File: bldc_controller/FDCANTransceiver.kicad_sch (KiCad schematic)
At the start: 4 parts, among them U9 TCAN1051HGVDRBRQ1

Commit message: might have fixed net issue, added dxf and svgs
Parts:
- gave numbers to parts that had none: 1
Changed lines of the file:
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@@
-    (stroke (width 0) (type default))
-  )
-  (polyline (pts (xy 99.06 55.88) (xy 99.06 130.81))
     (stroke (width 0) (type default))
   )
@@
     (stroke (width 0) (type default))
   )
-  (polyline (pts (xy 102.87 52.07) (xy 195.58 52.07))
-    (stroke (width 0) (type default))
-  )
-  (polyline (pts (xy 199.39 55.88) (xy 199.39 130.81))
-    (stroke (width 0) (type default))
-  )
   (wire (pts (xy 167.64 71.12) (xy 167.64 67.31))
     (stroke (width 0) (type default))
@@
     (stroke (width 0) (type default))
   )
-  (polyline (pts (xy 195.58 134.62) (xy 102.87 134.62))
-    (stroke (width 0) (type default))
-  )
   (bus (pts (xy 184.15 86.36) (xy 179.07 86.36))
     (stroke (width 0) (type default))
@@
     (stroke (width 0) (type default))
   )
+  (polyline (pts (xy 116.84 101.6) (xy 123.19 109.22))
+    (stroke (width 0) (type dot) (color 255 0 0 1))
+  )
   (wire (pts (xy 132.08 67.31) (xy 147.32 67.31))
     (stroke (width 0) (type default))
   )
-  (arc (start 102.87 134.62) (mid 100.1745 133.5055) (end 99.06 130.81)
-    (stroke (width 0) (type default))
-    (fill (type none))
-  )
-  (arc (start 199.39 130.81) (mid 198.2741 133.5041) (end 195.58 134.62)
-    (stroke (width 0) (type default))
-    (fill (type none))
-  )
-  (arc (start 195.58 52.07) (mid 198.2741 53.1859) (end 199.39 55.88)
-    (stroke (width 0) (type default))
-    (fill (type none))
-  )
-  (arc (start 99.06 55.88) (mid 100.1759 53.1859) (end 102.87 52.07)
-    (stroke (width 0) (type default))
-    (fill (type none))
-  )
-  (text_box "Back to Top Level"
-    (at 265.43 166.37 0) (size 19.05 14.605)
-    (stroke (width 0) (type default) (color 0 0 0 1))
-    (fill (type color) (color 0 0 0 0.1))
-    (effects (font (size 2.54 2.54) (thickness 0.508) bold (color 0 0 0 1)) (href "#1"))
+  (rectangle (start 81.28 49.53) (end 215.9 138.43)
+    (stroke (width 1) (type default) (color 200 200 200 1))
+    (fill (type none))
+  )
+  (rectangle (start 123.19 101.6) (end 130.81 109.22)
+    (stroke (width 0) (type dot) (color 255 0 0 1))
+    (fill (type none))
+  )
+  (text_box "LAYOUT NOTE:\nFD-CAN should be routed as a 120-ohm differential pair."
+    (at 181.61 101.6 0) (size 29.21 11.43)
+    (stroke (width 1) (type solid) (color 0 0 255 1))
+    (fill (type none))
+    (effects (font (face "Arial") (size 1.27 1.27) (thickness 0.4) bold (color 0 0 255 1)) (justify left top))
+  )
+  (text_box "LAYOUT NOTE:\nPlace close to FD-CAN connector if possible to reduce stub length."
+    (at 181.61 115.57 0) (size 29.21 11.43)
+    (stroke (width 1) (type solid) (color 0 0 255 1))
+    (fill (type none))
+    (effects (font (face "Arial") (size 1.27 1.27) (thickness 0.4) bold (color 0 0 255 1)) (justify left top))
+  )
+  (text_box "DESIGN NOTE:\n120-ohm termination in Interconnects sheet."
+    (at 85.09 115.57 0) (size 31.75 11.43)
+    (stroke (width 0.8) (type solid) (color 200 200 200 1))
+    (fill (type none))
+    (effects (font (face "Arial") (size 1.27 1.27) (color 0 0 0 1)) (justify left top))
+  )
+  (text_box "[16] Interface - FD-CAN"
+    (at 80.01 16.51 0) (size 137.16 12.7)
+    (stroke (width -0.0001) (type default))
+    (fill (type none))
+    (effects (font (face "Times New Roman") (size 6 6) (thickness 1.2) bold (color 162 22 34 1)))
   )
   (text_box "Fault Protected FD-CAN Transceiver"
-    (at 102.235 123.19 0) (size 94.615 9.525)
+    (at 82.55 127 0) (size 132.08 8.89)
     (stroke (width -0.0001) (type default))
     (fill (type none))
-    (effects (font (size 2.54 2.54) (color 0 0 0 1)) (justify bottom))
-  )
-  (text_box "Silent mode disabled"
-    (at 106.68 119.38 0) (size 13.97 5.08)
-    (stroke (width 0) (type default) (color 0 0 0 1))
-    (fill (type color) (color 191 240 255 1))
-    (effects (font (size 1.27 1.27) (color 0 0 0 1)) (justify left))
+    (effects (font (face "Times New Roman") (size 2.54 2.54) (thickness 0.508) bold (color 162 22 34 1)) (justify bottom))
+  )
+  (text_box "DESIGN NOTE:\nSilent mode disabled."
+    (at 85.09 101.6 0) (size 31.75 11.43)
+    (stroke (width 0.8) (type solid) (color 200 200 200 1))
+    (fill (type none))
+    (effects (font (face "Arial") (size 1.27 1.27) (color 0 0 0 1)) (justify left top))
   )
   (label "FDCAN_TX" (at 125.73 90.17 0) (fields_autoplaced)
@@
     (instances
       (project "bldc_controller"
-        (path "/0650c7a8-acba-429c-9f8e-eec0baf0bc1c/926acdff-90be-4f7b-9e19-9f96ee9f0571"
+        (path "/0650c7a8-acba-429c-9f8e-eec0baf0bc1c/fede4c36-00cc-4d3d-b71c-5243ba232202/95bf33d9-762c-4d08-af8b-3fad797ffaca"
           (reference "U9") (unit 1)
         )
@@
     (instances
       (project "bldc_controller"
-        (path "/0650c7a8-acba-429c-9f8e-eec0baf0bc1c/926acdff-90be-4f7b-9e19-9f96ee9f0571"
+        (path "/0650c7a8-acba-429c-9f8e-eec0baf0bc1c/fede4c36-00cc-4d3d-b71c-5243ba232202/95bf33d9-762c-4d08-af8b-3fad797ffaca"
           (reference "#PWR053") (unit 1)
         )
@@
     (instances
       (project "bldc_controller"
-        (path "/0650c7a8-acba-429c-9f8e-eec0baf0bc1c/926acdff-90be-4f7b-9e19-9f96ee9f0571"
+        (path "/0650c7a8-acba-429c-9f8e-eec0baf0bc1c/fede4c36-00cc-4d3d-b71c-5243ba232202/95bf33d9-762c-4d08-af8b-3fad797ffaca"
           (reference "#PWR052") (unit 1)
         )
@@
     (instances
       (project "bldc_controller"
-        (path "/0650c7a8-acba-429c-9f8e-eec0baf0bc1c/926acdff-90be-4f7b-9e19-9f96ee9f0571"
+        (path "/0650c7a8-acba-429c-9f8e-eec0baf0bc1c/fede4c36-00cc-4d3d-b71c-5243ba232202/95bf33d9-762c-4d08-af8b-3fad797ffaca"
           (reference "#PWR054") (unit 1)
         )
@@
     (instances
       (project "bldc_controller"
-        (path "/0650c7a8-acba-429c-9f8e-eec0baf0bc1c/926acdff-90be-4f7b-9e19-9f96ee9f0571"
+        (path "/0650c7a8-acba-429c-9f8e-eec0baf0bc1c/fede4c36-00cc-4d3d-b71c-5243ba232202/95bf33d9-762c-4d08-af8b-3fad797ffaca"
           (reference "#PWR056") (unit 1)
         )
@@
     (instances
       (project "bldc_controller"
-        (path "/0650c7a8-acba-429c-9f8e-eec0baf0bc1c/926acdff-90be-4f7b-9e19-9f96ee9f0571"
+        (path "/0650c7a8-acba-429c-9f8e-eec0baf0bc1c/fede4c36-00cc-4d3d-b71c-5243ba232202/95bf33d9-762c-4d08-af8b-3fad797ffaca"
           (reference "C93") (unit 1)
         )
@@
     (instances
       (project "bldc_controller"
-        (path "/0650c7a8-acba-429c-9f8e-eec0baf0bc1c/926acdff-90be-4f7b-9e19-9f96ee9f0571"
+        (path "/0650c7a8-acba-429c-9f8e-eec0baf0bc1c/fede4c36-00cc-4d3d-b71c-5243ba232202/95bf33d9-762c-4d08-af8b-3fad797ffaca"
           (reference "#PWR055") (unit 1)
         )
@@
     (instances
       (project "bldc_controller"
-        (path "/0650c7a8-acba-429c-9f8e-eec0baf0bc1c/926acdff-90be-4f7b-9e19-9f96ee9f0571"
+        (path "/0650c7a8-acba-429c-9f8e-eec0baf0bc1c/fede4c36-00cc-4d3d-b71c-5243ba232202/95bf33d9-762c-4d08-af8b-3fad797ffaca"
           (reference "C92") (unit 1)
         )
@@
   (symbol (lib_id "Device:R") (at 127 105.41 0) (unit 1)
     (in_bom yes) (on_board yes) (dnp no) (fields_autoplaced)
-    (property "Reference" "R?" (at 129.54 104.14 0)
+    (property "Reference" "R29" (at 129.54 104.14 0)
       (effects (font (size 1.27 1.27)) (justify left))
     )
@@
     (instances
       (project "bldc_controller"
-        (path "/0650c7a8-acba-429c-9f8e-eec0baf0bc1c/ce1ea51b-4118-4fb5-9a41-40670da86eb7"
-          (reference "R?") (unit 1)
-        )
-        (path "/0650c7a8-acba-429c-9f8e-eec0baf0bc1c/926acdff-90be-4f7b-9e19-9f96ee9f0571"
+        (path "/0650c7a8-acba-429c-9f8e-eec0baf0bc1c/fede4c36-00cc-4d3d-b71c-5243ba232202/95bf33d9-762c-4d08-af8b-3fad797ffaca"
           (reference "R29") (unit 1)
         )

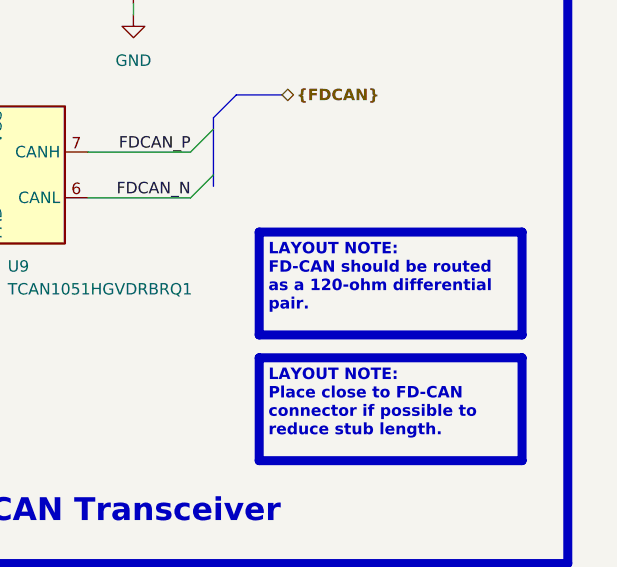
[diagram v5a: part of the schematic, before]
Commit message: added chassis connection to connector MP. Might need to change design rules to be compatible with low-cost PCBWay
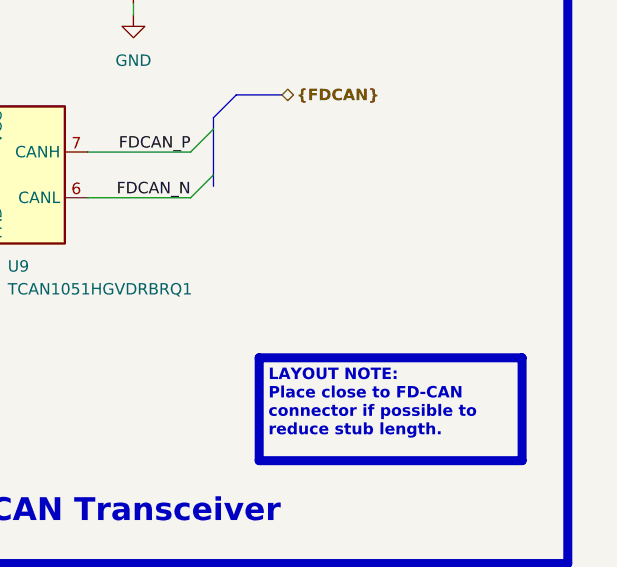
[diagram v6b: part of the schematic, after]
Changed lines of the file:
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@@
   (junction (at 132.08 67.31) (diameter 0) (color 0 0 0 0)
   )
-  (junction (at 147.32 110.49) (diameter 0) (color 0 0 0 0)
+  (junction (at 147.32 110.49) (diameter 0) (color 0 0 0 1)
   )
   (junction (at 167.64 67.31) (diameter 0) (color 0 0 0 0)
   )
-  (junction (at 127 110.49) (diameter 0) (color 0 0 0 0)
+  (junction (at 127 110.49) (diameter 0) (color 0 0 0 1)
   )
   (bus_entry (at 176.53 95.25) (size -2.54 2.54)
@@
   )
   (wire (pts (xy 127 110.49) (xy 147.32 110.49))
-    (stroke (width 0) (type default))
+    (stroke (width 0.381) (type default) (color 0 0 0 1))
   )
   (bus (pts (xy 176.53 90.17) (xy 176.53 95.25))
@@
   )
   (wire (pts (xy 147.32 110.49) (xy 152.4 110.49))
-    (stroke (width 0) (type default))
+    (stroke (width 0.381) (type default) (color 0 0 0 1))
   )
   (bus (pts (xy 176.53 95.25) (xy 176.53 96.52))
@@
   )
   (wire (pts (xy 132.08 77.47) (xy 132.08 76.2))
-    (stroke (width 0) (type default))
+    (stroke (width 0.381) (type default) (color 0 0 0 1))
   )
   (wire (pts (xy 152.4 67.31) (xy 152.4 85.09))
@@
   )
   (wire (pts (xy 147.32 105.41) (xy 147.32 110.49))
-    (stroke (width 0) (type default))
+    (stroke (width 0.381) (type default) (color 0 0 0 1))
   )
   (wire (pts (xy 132.08 71.12) (xy 132.08 67.31))
@@
   )
   (wire (pts (xy 167.64 77.47) (xy 167.64 76.2))
-    (stroke (width 0) (type default))
+    (stroke (width 0.381) (type default) (color 0 0 0 1))
   )
   (bus (pts (xy 123.19 90.17) (xy 123.19 91.44))
@@
   )
   (wire (pts (xy 127 113.03) (xy 127 110.49))
-    (stroke (width 0) (type default))
+    (stroke (width 0.381) (type default) (color 0 0 0 1))
   )
   (wire (pts (xy 127 109.22) (xy 127 110.49))
-    (stroke (width 0) (type default))
+    (stroke (width 0.381) (type default) (color 0 0 0 1))
   )
   (wire (pts (xy 152.4 110.49) (xy 152.4 105.41))
-    (stroke (width 0) (type default))
+    (stroke (width 0.381) (type default) (color 0 0 0 1))
   )
   (wire (pts (xy 132.08 64.77) (xy 132.08 67.31))
@@
     (fill (type none))
   )
-  (text_box "LAYOUT NOTE:\nFD-CAN should be routed as a 120-ohm differential pair."
-    (at 181.61 101.6 0) (size 29.21 11.43)
-    (stroke (width 1) (type solid) (color 0 0 255 1))
-    (fill (type none))
-    (effects (font (face "Arial") (size 1.27 1.27) (thickness 0.4) bold (color 0 0 255 1)) (justify left top))
-  )
   (text_box "LAYOUT NOTE:\nPlace close to FD-CAN connector if possible to reduce stub length."
